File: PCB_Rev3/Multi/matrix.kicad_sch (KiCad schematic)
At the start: 141 parts

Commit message: Integrated to Rev3
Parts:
- removed S28-1: MX1A, PCM_Switch_Keyboard_Hotswap_Kailh:SW_Hotswap_Kailh_MX_Plated_1.50u_90deg, symbol Switch:SW_Push
- added D14-2, D66, D67: DIODE, Diode_SMD:D_SOD-123, symbol Device:D
- added S14-x1, S29-x2, S41-x1, S41-x2, S60-x3, S60-x4: MX_stab, PCM_Mounting_Keyboard_Stabilizer:Stabilizer_Cherry_MX_2.00u, symbol PCM_marbastlib-mx:MX_stab
- added S28: MX1A, PCM_Switch_Keyboard_Hotswap_Kailh:SW_Hotswap_Kailh_MX_Plated_1.50u_90deg, symbol Switch:SW_Push
- added S60-1-a1: MX1A, PCM_Switch_Keyboard_Hotswap_Kailh:SW_Hotswap_Kailh_MX_Plated_2.25u, symbol Switch:SW_Push
- added S60-1-b1: MX1A, PCM_Switch_Keyboard_Hotswap_Kailh:SW_Hotswap_Kailh_MX_Plated_2.75u, symbol Switch:SW_Push
- added S60-x1: MX_stab, PCM_Mounting_Keyboard_Stabilizer:Stabilizer_Cherry_MX_6.25u, symbol PCM_marbastlib-mx:MX_stab
- added S60-x2: MX_stab, PCM_Mounting_Keyboard_Stabilizer:Stabilizer_Cherry_MX_7.00u, symbol PCM_marbastlib-mx:MX_stab
- added S63-2: MX1A, PCM_Switch_Keyboard_Hotswap_Kailh:SW_Hotswap_Kailh_MX_Plated_1.25u, symbol Switch:SW_Push
- added S65: MX1A, PCM_Switch_Keyboard_Hotswap_Kailh:SW_Hotswap_Kailh_MX_Plated_6.00u, symbol Switch:SW_Push
- S122: renamed from S60; footprint PCM_Switch_Keyboard_Hotswap_Kailh:SW_Hotswap_Kailh_MX_Plated_6.25u -> PCM_Switch_Keyboard_Hotswap_Kailh:SW_Hotswap_Kailh_MX_Plated_1.25u
- renumbered D34 to D100, D35 to D101, D36 to D102, D37 to D103, D38 to D104, D39 to D105, D40 to D106, D41 to D107, D44 to D110, D45 to D111, D48 to D114, D49 to D115, D50 to D116, D51 to D117, D52 to D118, D53 to D119, D54 to D120, D55 to D121, D58 to D124, D59 to D125, D60 to D126, D61 to D128, D62 to D130, D63 to D131, D64 to D132, D65 to D133, D29 to D28, D42 to D41, D43 to D42, D46 to D45, D47 to D46, D56 to D55, D57 to D56, D2 to D68, D3 to D69, D4 to D70, D5 to D71, D6 to D72, D7 to D73, D8 to D74, D9 to D75, D10 to D76, D11 to D77, D12 to D78, D13 to D79, D14 to D80, D15 to D81, D16 to D82, D17 to D83, D18 to D84, D19 to D85, D20 to D86, D21 to D87, D22 to D88, D23 to D89, D24 to D90, D25 to D91, D26 to D92, D27 to D93, D28 to D94, D30 to D96, D31 to D97, D32 to D98, D33 to D99, S34 to S100, S35 to S101, S36 to S102, S37 to S103, S38 to S104, S39 to S105, S40 to S106, S44 to S109, S47 to S112, S48 to S113, S49 to S114, S50 to S115, S51 to S116, S52 to S117, S53 to S118, S54 to S119, S57 to S124, S61 to S126, S42 to S14-3, S41-1 to S41, S41 to S41-2, S28 to S42, S43-1 to S43-2, S57-1 to S57-2, S58-1 to S58-2, S59-1 to S59-2, S60-1 to S60-2, S61-1 to S61-2, S62-1 to S62-2, S64-1 to S64-2, S1 to S66, S2 to S67, S3 to S68, S4 to S69, S5 to S70, S6 to S71, S7 to S72, S8 to S73, S9 to S74, S10 to S75, S11 to S76, S12 to S77, S13 to S78, S14 to S79, S15 to S80, S16 to S81, S17 to S82, S18 to S83, S19 to S84, S20 to S85, S21 to S86, S22 to S87, S23 to S88, S24 to S89, S25 to S90, S26 to S91, S27 to S92, S29 to S95, S30 to S96, S31 to S97, S32 to S98, S33 to S99
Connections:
- net row_4 is gone; now on net col_0: D124.1 (K), D125.1 (K), D126.1 (K), D128.1 (K), D130.1 (K), D131.1 (K), D132.1 (K), D133.1 (K)
- net col_0: now also S43-2.1, S43.2, D66.1 (K), D67.1 (K); no longer S43-2.2, S43.1
- net col_1: now also S58-2.1, S58.2; no longer S58-2.2, S58.1
- net col_10: now also S61-2.1; no longer S61-2.2
- net col_11: now also S62-2.1, S62.2; no longer S62-2.2, S62.1
- net col_12: now also S41-2.1, S55-1.1, S55.2, S63.2, S63-2.1; no longer S41-2.2, S55-1.2, S55.1, S63.1
- net col_13: now also S14-1.1, S42.1, S64-2.1, S64.2, S28.2; no longer S14-1.2, S14-3.1, S42.2, S64-2.2, S64.1
- net col_2: now also S59.2; no longer S59-2.2, S59.1
- net col_4: now also S60-1-a1.2
- net col_6: now also S65.2
- net col_8: now also S60-1-b1.2
- net row_0: now also D14-2.1 (K)
- net at D81.2 (A), S79.1: now also S14-1.2; no longer S14-1.1
- net at D128.2 (A), S122.1, S60-2.2: now also S65.1
- net at D41.2 (A), S41.1: now also S41-2.2; no longer S41-2.1
- net at D28.2 (A): now also S28.1; no longer S42.1
- net at D132.2 (A): now also S63.1, S63-2.2; no longer S63.2
- net at D42.2 (A): now also S42.2; no longer S14-3.2
- net at D130.2 (A), S126.1: now also S61-2.2; no longer S61-2.1
- new net: D133.2 (A), S64-2.2, S64.1
- new net: D125.2 (A), S58-2.2, S58.1
- new net: D110.2 (A), S43-2.2, S43.1
- new net: D55.2 (A), S55-1.2, S55.1
- new net: D131.2 (A), S62-2.2, S62.1
- new net: D14-2.2 (A), S14-3.2
- new net: D67.2 (A), S60-1-b1.1
- new net: D66.2 (A), S60-1-a1.1
- new net: D126.2 (A), S59.1
- new net col_14: S14-3.1
- now unconnected: S59-2.1
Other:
- note added: "1.25u/2.25u LSFT"
- note added: "1.75u/2.75u RSFT"
- note added: "1u/1.5u BOTTOM"
- note added: "2.25u/ISO/BA ENTER"
- note added: "2u/1u BKSP"
- note added: "6u/6.25u/7u ? 2.25u/1.25u/2.75u SPCACE"
- note added: "Caps/ Stepped Caps"
- moved on the sheet: D110, D124, D125, D96, S122, S124, S14-1, S14-3, S29-1, S41, S41-2, S42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

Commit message: muliti layout
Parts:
- renumbered D76 to D10, D77 to D11, D78 to D12, D79 to D13, D80 to D14, D14-2 to D14-1, D81 to D15, D82 to D16, D83 to D17, D84 to D18, D85 to D19, D68 to D2, D86 to D20, D87 to D21, D88 to D22, D89 to D23, D90 to D24, D91 to D25, D92 to D26, D93 to D27, D94 to D28, D28 to D29, D69 to D3, D96 to D30, D97 to D31, D98 to D32, D99 to D33, D100 to D34, D101 to D35, D102 to D36, D103 to D37, D104 to D38, D105 to D39, D70 to D4, D106 to D40, D107 to D41, D41 to D42, D42 to D43, D110 to D44, D111 to D45, D45 to D46, D46 to D47, D114 to D48, D115 to D49, D71 to D5, D116 to D50, D117 to D51, D118 to D52, D119 to D53, D120 to D54, D121 to D55, D55 to D56, D56 to D57, D124 to D58, D125 to D59, D72 to D6, D126 to D60, D66 to D61, D128 to D62, D67 to D63, D130 to D64, D131 to D65, D132 to D66, D133 to D67, D73 to D7, D74 to D8, D75 to D9, S66 to S1, S75 to S10, S76 to S11, S77 to S12, S78 to S13, S79 to S14, S14-3 to S14-2, S80 to S15, S81 to S16, S82 to S17, S83 to S18, S84 to S19, S67 to S2, S85 to S20, S86 to S21, S87 to S22, S88 to S23, S89 to S24, S90 to S25, S91 to S26, S92 to S27, S42 to S29, S29-x2 to S29-x1, S68 to S3, S95 to S30, S96 to S31, S97 to S32, S98 to S33, S99 to S34, S100 to S35, S101 to S36, S102 to S37, S103 to S38, S104 to S39, S69 to S4, S105 to S40, S106 to S41, S41-2 to S41-1, S41-x2 to S41-x1, S41-x1 to S41-x2, S41 to S42, S43-2 to S43-1, S109 to S44, S112 to S47, S113 to S48, S114 to S49, S70 to S5, S115 to S50, S116 to S51, S117 to S52, S118 to S53, S119 to S54, S122 to S57, S57-2 to S57-1, S65 to S58, S58-2 to S58-1, S124 to S59, S59-2 to S59-1, S71 to S6, S59 to S60, S60-2 to S60-1, S60-x3 to S60-x2, S60-x2 to S60-x3, S126 to S61, S61-2 to S61-1, S62-2 to S62-1, S63-2 to S63-1, S64-2 to S64-1, S58 to S65, S72 to S7, S73 to S8, S74 to S9

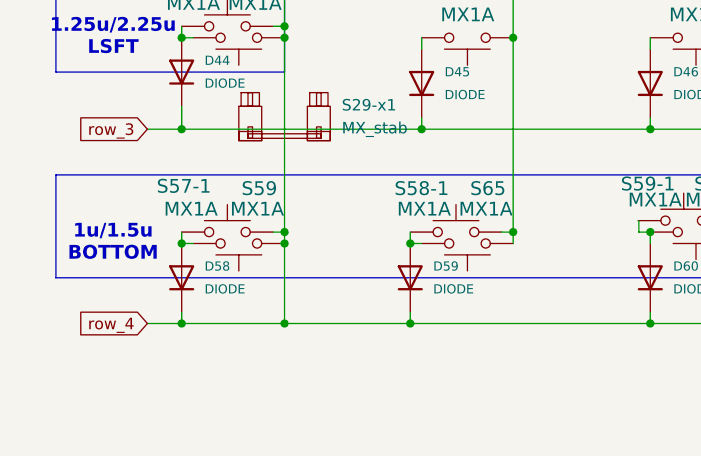
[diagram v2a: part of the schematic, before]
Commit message: With the basic layout and wiring completed, a simple DRC (Digital Router Control) process is performed.
There is an issue with the satellite axis position that needs to be addressed, and there is also an issue with some pad overlap that needs to be resolved.
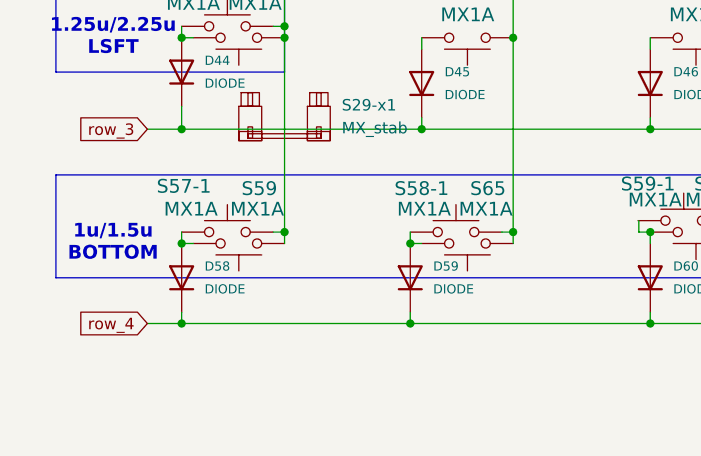
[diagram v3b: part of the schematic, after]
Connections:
- net col_0: no longer D58.1 (K), D59.1 (K), D60.1 (K), D61.1 (K), D62.1 (K), D63.1 (K), D64.1 (K), D65.1 (K), D66.1 (K), D67.1 (K)
- new net row_4: D58.1 (K), D59.1 (K), D60.1 (K), D61.1 (K), D62.1 (K), D63.1 (K), D64.1 (K), D65.1 (K), D66.1 (K), D67.1 (K)
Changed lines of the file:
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@@
-	)
-	(junction
-		(at 53.34 157.48)
-		(diameter 0)
-		(color 0 0 0 0)
 	)
 	(junction
@@
 	)
 	(junction
-		(at 53.34 148.59)
-		(diameter 0)
-		(color 0 0 0 0)
-	)
-	(junction
 		(at 144.78 114.3)
 		(diameter 0)
@@
 	(wire
 		(pts
-			(xy 53.34 157.48) (xy 67.31 157.48)
+			(xy 41.91 157.48) (xy 67.31 157.48)
 		)
 		(stroke
@@
 	(wire
 		(pts
-			(xy 41.91 157.48) (xy 53.34 157.48)
-		)
-		(stroke
-			(width 0)
-			(type default)
-		)
-	)
-	(wire
-		(pts
 			(xy 358.14 124.46) (xy 358.14 125.73)
 		)
@@
 		)
 		(stroke
-			(width 0)
-			(type default)
-		)
-	)
-	(wire
-		(pts
-			(xy 53.34 148.59) (xy 53.34 157.48)
-		)
-		(stroke

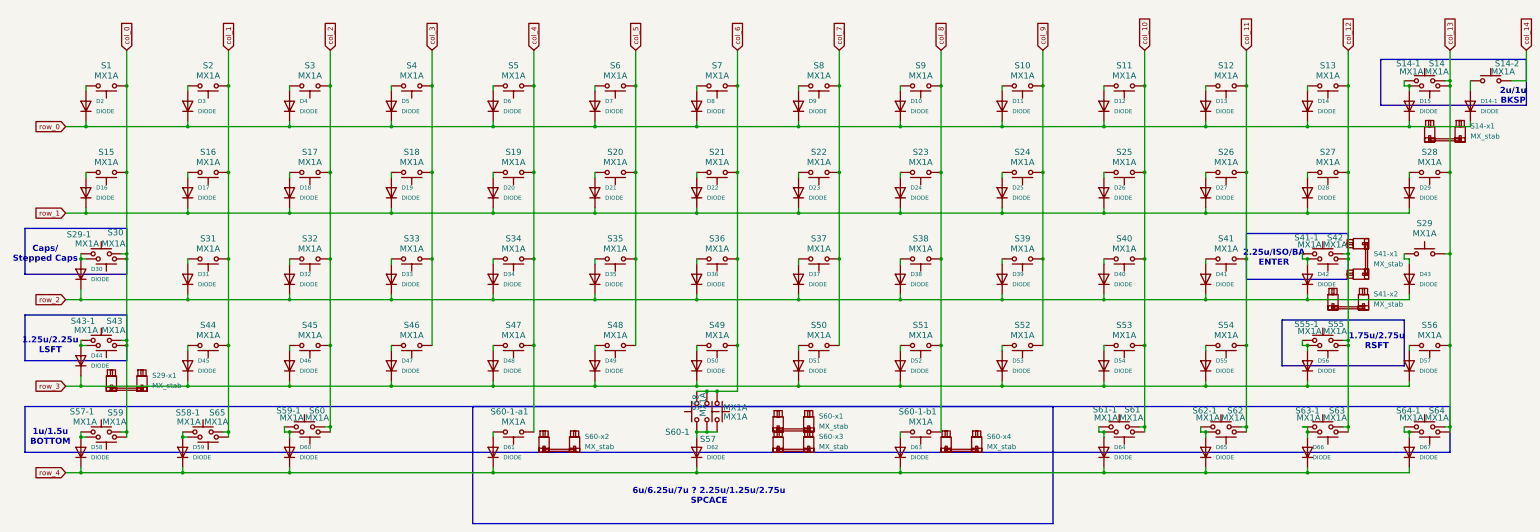
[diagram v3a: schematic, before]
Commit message: Delete RGB
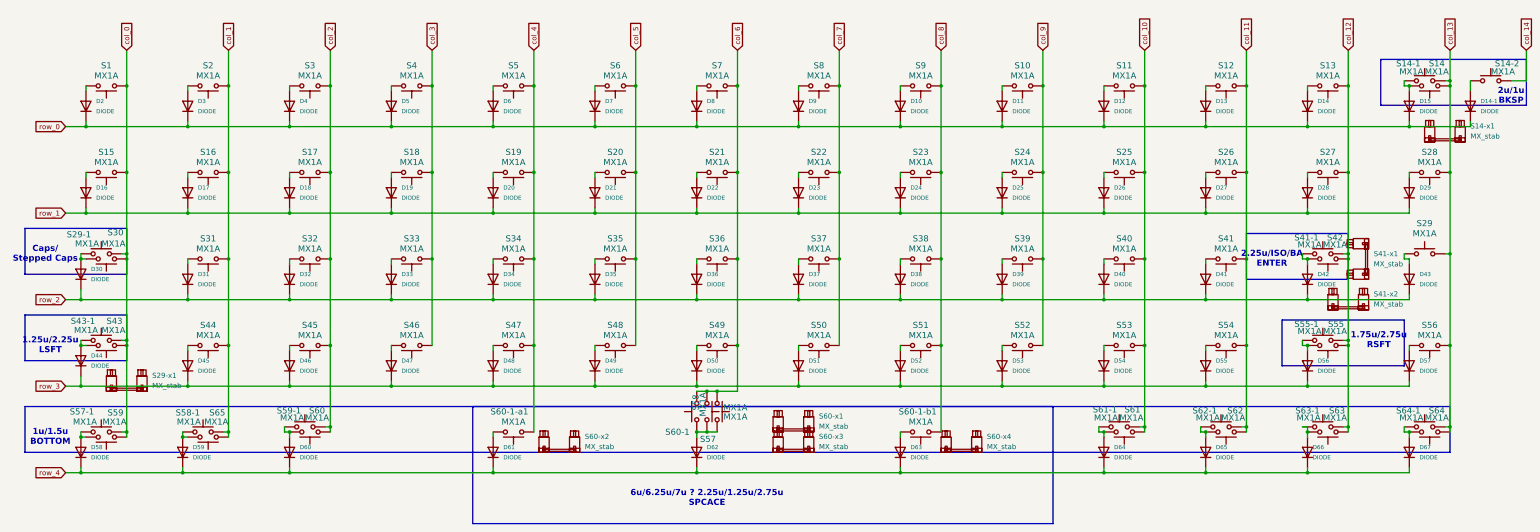
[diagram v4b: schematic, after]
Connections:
- net col_2: now also S59-1.1
- net at S59-1.2: now also D60.2 (A), S60.1
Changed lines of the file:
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@@
 	(text "2.25u/ISO/BA\nENTER\n"
 		(exclude_from_sim no)
-		(at 339.598 103.886 0)
+		(at 339.09 104.14 0)
 		(effects
 			(font
@@
 	(text "6u/6.25u/7u ? 2.25u/1.25u/2.75u\nSPCACE\n"
 		(exclude_from_sim no)
-		(at 198.628 163.322 0)
+		(at 198.12 163.83 0)
 		(effects
 			(font
@@
 	(text "2u/1u\nBKSP\n"
 		(exclude_from_sim no)
-		(at 399.288 63.5 0)
+		(at 398.78 63.5 0)
 		(effects
 			(font
@@
 	(text "1.75u/2.75u\nRSFT"
 		(exclude_from_sim no)
-		(at 365.252 124.714 0)
+		(at 365.76 124.46 0)
 		(effects
 			(font
@@
 	(symbol
 		(lib_id "Switch:SW_Push")
-		(at 97.6921 146.05 0)
+		(at 97.79 146.05 0)
 		(mirror y)
 		(unit 1)
@@
 		(dnp no)
 		(property "Reference" "S59-1"
-			(at 93.726 141.986 0)
+			(at 93.8239 141.986 0)
 			(effects
 				(font
@@
 		)
 		(property "Value" "MX1A"
-			(at 94.488 143.764 0)
+			(at 94.5859 143.764 0)
 			(effects
 				(font
@@
 		)
 		(property "Footprint" "PCM_Switch_Keyboard_Hotswap_Kailh:SW_Hotswap_Kailh_MX_Plated_1.50u"
-			(at 97.6921 140.97 0)
+			(at 97.79 140.97 0)
 			(effects
 				(font
@@
 		)
 		(property "Datasheet" "~"
-			(at 97.6921 140.97 0)
+			(at 97.79 140.97 0)
 			(effects
 				(font
@@
 		)
 		(property "Description" "Push button switch, generic, two pins"
-			(at 97.6921 146.05 0)
+			(at 97.79 146.05 0)
 			(effects
 				(font

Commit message: Add more split space
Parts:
- added S60-1-a2, S60-1-b2: MX1A, PCM_Switch_Keyboard_Hotswap_Kailh:SW_Hotswap_Kailh_MX_Plated_3.00u, symbol Switch:SW_Push
- added S60-x5, S60-x6: MX_stab, PCM_Mounting_Keyboard_Stabilizer:Stabilizer_Cherry_MX_2.00u, symbol PCM_marbastlib-mx:MX_stab
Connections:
- net col_4: now also S60-1-a2.1
- net col_8: now also S60-1-b2.1
- net at D63.2 (A), S60-1-b1.1: now also S60-1-b2.2
- net at D61.2 (A), S60-1-a1.1: now also S60-1-a2.2

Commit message: Change charger and power supply
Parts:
- S62-1: footprint PCM_Switch_Keyboard_Hotswap_Kailh:SW_Hotswap_Kailh_MX_Plated_1.00u -> PCM_Switch_Keyboard_Hotswap_Kailh:SW_Hotswap_Kailh_MX_Plated_1.50u
- S63-1: footprint PCM_Switch_Keyboard_Hotswap_Kailh:SW_Hotswap_Kailh_MX_Plated_1.25u -> PCM_Switch_Keyboard_Hotswap_Kailh:SW_Hotswap_Kailh_MX_Plated_1.00u
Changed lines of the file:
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@@
 			)
 		)
-		(property "Footprint" "PCM_Switch_Keyboard_Hotswap_Kailh:SW_Hotswap_Kailh_MX_Plated_1.25u"
+		(property "Footprint" "PCM_Switch_Keyboard_Hotswap_Kailh:SW_Hotswap_Kailh_MX_Plated_1.00u"
 			(at 351.79 140.97 0)
 			(effects
@@
 			)
 		)
-		(property "Footprint" "PCM_Switch_Keyboard_Hotswap_Kailh:SW_Hotswap_Kailh_MX_Plated_1.00u"
+		(property "Footprint" "PCM_Switch_Keyboard_Hotswap_Kailh:SW_Hotswap_Kailh_MX_Plated_1.50u"
 			(at 326.39 140.97 0)
 			(effects

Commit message: Merge changes
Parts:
- removed S61-1: MX1A, PCM_Switch_Keyboard_Hotswap_Kailh:SW_Hotswap_Kailh_MX_Plated_1.50u, symbol Switch:SW_Push
- added S55-x1: MX_stab, PCM_Mounting_Keyboard_Stabilizer:Stabilizer_Cherry_MX_2.00u, symbol PCM_marbastlib-mx:MX_stab
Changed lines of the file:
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@@
 	)
 	(junction
-		(at 297.18 147.32)
-		(diameter 0)
-		(color 0 0 0 0)
-	)
-	(junction
 		(at 144.78 147.32)
 		(diameter 0)
@@
 	)
 	(junction
-		(at 307.34 146.05)
-		(diameter 0)
-		(color 0 0 0 0)
-	)
-	(junction
 		(at 78.74 147.32)
 		(diameter 0)
@@
 	(wire
 		(pts
-			(xy 295.91 146.05) (xy 295.91 147.32)
-		)
-		(stroke
-			(width 0)
-			(type default)
-		)
-	)
-	(wire
-		(pts
 			(xy 104.14 60.96) (xy 104.14 82.55)
 		)
@@
 	(wire
 		(pts
-			(xy 307.34 125.73) (xy 307.34 146.05)
-		)
-		(stroke
-			(width 0)
-			(type default)
-		)
-	)
-	(wire
-		(pts
 			(xy 144.78 147.32) (xy 144.78 148.59)
 		)
@@
 	(wire
 		(pts
-			(xy 307.34 146.05) (xy 307.34 147.32)
+			(xy 307.34 125.73) (xy 307.34 147.32)
 		)
 		(stroke
@@
 	(wire
 		(pts
-			(xy 295.91 147.32) (xy 297.18 147.32)
-		)
-		(stroke
-			(width 0)
-			(type default)
-		)
-	)
-	(wire
-		(pts
 			(xy 246.38 92.71) (xy 271.78 92.71)
 		)
@@
 	(wire
 		(pts
-			(xy 306.07 146.05) (xy 307.34 146.05)
-		)
-		(stroke
-			(width 0)
-			(type default)
-		)
-	)
-	(wire
-		(pts
 			(xy 93.98 114.3) (xy 119.38 114.3)
 		)
@@
 	)
 	(symbol
+		(lib_id "PCM_marbastlib-mx:MX_stab")
+		(at 363.22 128.27 0)
+		(unit 1)
+		(exclude_from_sim no)
+		(in_bom yes)
+		(on_board yes)
+		(dnp no)
+		(fields_autoplaced yes)
+		(property "Reference" "S55-x1"
+			(at 369.57 126.8729 0)
+			(effects
+				(font
+					(size 1.27 1.27)
+				)
+				(justify left)
+			)
+		)
+		(property "Value" "MX_stab"
+			(at 369.57 129.4129 0)
+			(effects
+				(font
+					(size 1.27 1.27)
+				)
+				(justify left)
+			)
+		)
+		(property "Footprint" "PCM_Mounting_Keyboard_Stabilizer:Stabilizer_Cherry_MX_2.00u"
+			(at 363.22 128.27 0)
+			(effects
+				(font
+					(size 1.27 1.27)
+				)
+				(hide yes)
+			)
+		)
+		(property "Datasheet" ""
+			(at 363.22 128.27 0)
+			(effects
+				(font
+					(size 1.27 1.27)
+				)
+				(hide yes)
+			)
+		)
+		(property "Description" "Cherry MX-style stabilizer"
+			(at 363.22 128.27 0)
+			(effects
+				(font
+					(size 1.27 1.27)
+				)
+				(hide yes)
+			)
+		)
+		(instances
+			(project "PH60_Rev3"
+				(path "/dca0f898-8fdb-4522-a51d-f4f4238906e7/dc5cd3b2-ef82-41de-b720-71645d542746"
+					(reference "S55-x1")
+					(unit 1)
+				)
+			)
+		)
+	)
+	(symbol
 		(lib_id "Switch:SW_Push")
 		(at 124.46 104.14 0)
@@
 					(unit 1)
 				)
-			)
-		)
-	)
-	(symbol
-		(lib_id "Switch:SW_Push")
-		(at 300.99 146.05 0)
-		(mirror y)
-		(unit 1)
-		(exclude_from_sim no)
-		(in_bom yes)
-		(on_board yes)
-		(dnp no)
-		(property "Reference" "S61-1"
-			(at 297.434 141.732 0)
-			(effects
-				(font
-					(size 1.524 1.524)
-				)
-			)
-		)
-		(property "Value" "MX1A"
-			(at 297.688 143.764 0)
-			(effects
-				(font
-					(size 1.524 1.524)
-				)
-			)
-		)
-		(property "Footprint" "PCM_Switch_Keyboard_Hotswap_Kailh:SW_Hotswap_Kailh_MX_Plated_1.50u"
-			(at 300.99 140.97 0)
-			(effects
-				(font
-					(size 1.27 1.27)
-				)
-				(hide yes)
-			)
-		)
-		(property "Datasheet" "~"
-			(at 300.99 140.97 0)
-			(effects
-				(font
-					(size 1.27 1.27)
-				)
-				(hide yes)
-			)
-		)
-		(property "Description" "Push button switch, generic, two pins"
-			(at 300.99 146.05 0)
-			(effects
-				(font
-					(size 1.27 1.27)
-				)
-				(hide yes)
-			)
-		)
-		(pin "2"
-		)
-		(pin "1"
-		)
-		(instances
-			(project "PH60_Rev3"
-				(path "/dca0f898-8fdb-4522-a51d-f4f4238906e7/dc5cd3b2-ef82-41de-b720-71645d542746"
-					(reference "S61-1")
-					(unit 1)
-				)

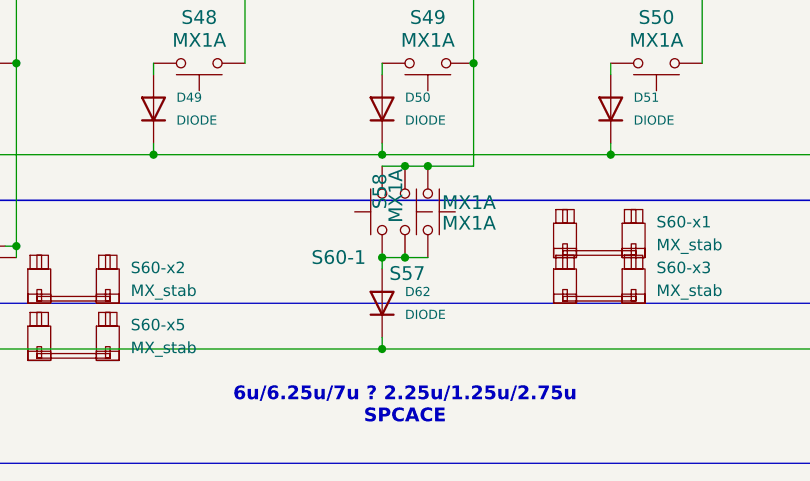
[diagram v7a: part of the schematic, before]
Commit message: Fix split space and remove 6U HHKB
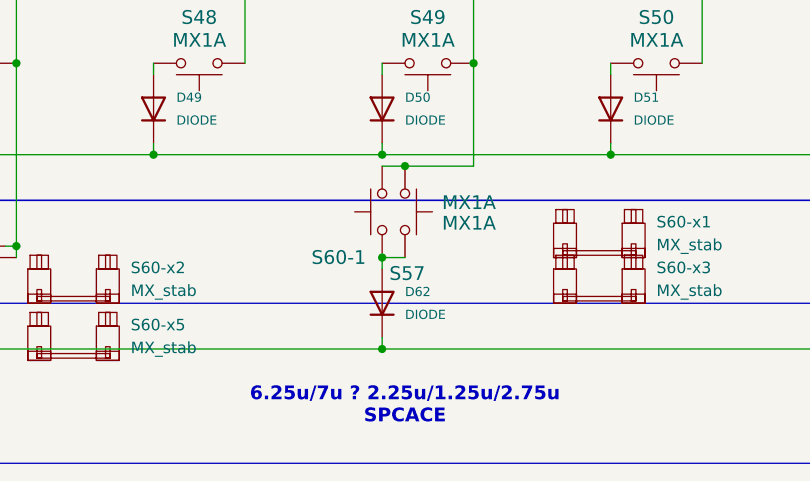
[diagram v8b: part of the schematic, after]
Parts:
- removed S58: MX1A, PCM_Switch_Keyboard_Hotswap_Kailh:SW_Hotswap_Kailh_MX_Plated_6.00u, symbol Switch:SW_Push
- S60-x2, S60-x5: now left out of the parts list
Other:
- note added: "6.25u/7u ? 2.25u/1.25u/2.75u SPCACE"
- note removed: "6u/6.25u/7u ? 2.25u/1.25u/2.75u SPCACE"
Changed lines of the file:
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@@
 		)
 	)
-	(text "6u/6.25u/7u ? 2.25u/1.25u/2.75u\nSPCACE\n"
+	(text "6.25u/7u ? 2.25u/1.25u/2.75u\nSPCACE\n"
 		(exclude_from_sim no)
 		(at 198.12 163.83 0)
@@
 	)
 	(junction
-		(at 198.12 147.32)
-		(diameter 0)
-		(color 0 0 0 0)
-	)
-	(junction
 		(at 332.74 82.55)
 		(diameter 0)
@@
 	)
 	(junction
-		(at 200.66 137.16)
-		(diameter 0)
-		(color 0 0 0 0)
-	)
-	(junction
 		(at 78.74 104.14)
 		(diameter 0)
@@
 	(wire
 		(pts
-			(xy 200.66 137.16) (xy 205.74 137.16)
+			(xy 198.12 137.16) (xy 205.74 137.16)
 		)
 		(stroke
@@
 	(wire
 		(pts
-			(xy 198.12 137.16) (xy 200.66 137.16)
-		)
-		(stroke
-			(width 0)
-			(type default)
-		)
-	)
-	(wire
-		(pts
 			(xy 43.18 69.85) (xy 43.18 71.12)
 		)
@@
 	(wire
 		(pts
-			(xy 198.12 147.32) (xy 200.66 147.32)
-		)
-		(stroke
-			(width 0)
-			(type default)
-		)
-	)
-	(wire
-		(pts
 			(xy 246.38 156.21) (xy 246.38 157.48)
 		)
@@
 	)
 	(symbol
-		(lib_id "Switch:SW_Push")
-		(at 200.66 142.24 270)
-		(mirror x)
-		(unit 1)
-		(exclude_from_sim no)
-		(in_bom yes)
-		(on_board yes)
-		(dnp no)
-		(property "Reference" "S58"
-			(at 195.326 139.954 0)
-			(effects
-				(font
-					(size 1.524 1.524)
-				)
-			)
-		)
-		(property "Value" "MX1A"
-			(at 197.104 140.462 0)
-			(effects
-				(font
-					(size 1.524 1.524)
-				)
-			)
-		)
-		(property "Footprint" "PCM_Switch_Keyboard_Hotswap_Kailh:SW_Hotswap_Kailh_MX_Plated_6.00u"
-			(at 205.74 142.24 0)
-			(effects
-				(font
-					(size 1.27 1.27)
-				)
-				(hide yes)
-			)
-		)
-		(property "Datasheet" "~"
-			(at 205.74 142.24 0)
-			(effects
-				(font
-					(size 1.27 1.27)
-				)
-				(hide yes)
-			)
-		)
-		(property "Description" "Push button switch, generic, two pins"
-			(at 200.66 142.24 0)
-			(effects
-				(font
-					(size 1.27 1.27)
-				)
-				(hide yes)
-			)
-		)
-		(pin "2"
-		)
-		(pin "1"
-		)
-		(instances
-			(project "PH60_Rev3"
-				(path "/dca0f898-8fdb-4522-a51d-f4f4238906e7/dc5cd3b2-ef82-41de-b720-71645d542746"
-					(reference "S58")
-					(unit 1)
-				)
-			)
-		)
-	)
-	(symbol
 		(lib_id "Device:D")
 		(at 373.38 109.22 90)
@@
 		(unit 1)
 		(exclude_from_sim no)
-		(in_bom yes)
+		(in_bom no)
 		(on_board yes)
 		(dnp no)
@@
 		(unit 1)
 		(exclude_from_sim no)
-		(in_bom yes)
+		(in_bom no)
 		(on_board yes)
 		(dnp no)
